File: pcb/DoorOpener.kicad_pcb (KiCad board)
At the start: 2 copper layers, 50.8 x 37.8 mm, 7 parts, among them SW1 POWER, SW2 Button, U2 ESP-01v090

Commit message: Prepare for milling the pcb
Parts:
- removed H2: MountingHole, MountingHole:MountingHole_3mm
- moved H1 14.6 mm to (76.0, 140.7)
- moved SW2 13.4 mm to (79.0, 125.6), turned to -90 degrees
- moved U2 8.07 mm to (84.1, 144.5)
- moved D1 7.12 mm to (85.0, 153.9)
- moved SW1 1.14 mm to (85.2, 124.6)
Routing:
- net Net-(SW2-Pad1): track 24.7 -> 16.0 mm
- net +3V3: track 31.5 -> 35.0 mm
- net Net-(D1-Pad4): track 16.5 -> 13.1 mm
- net Net-(BT1-Pad1): track 9.79 -> 8.40 mm
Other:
- board size 50.8 x 37.8 mm -> 48 x 37.7 mm
- board text added: "v0.1 - 17.11.2022"

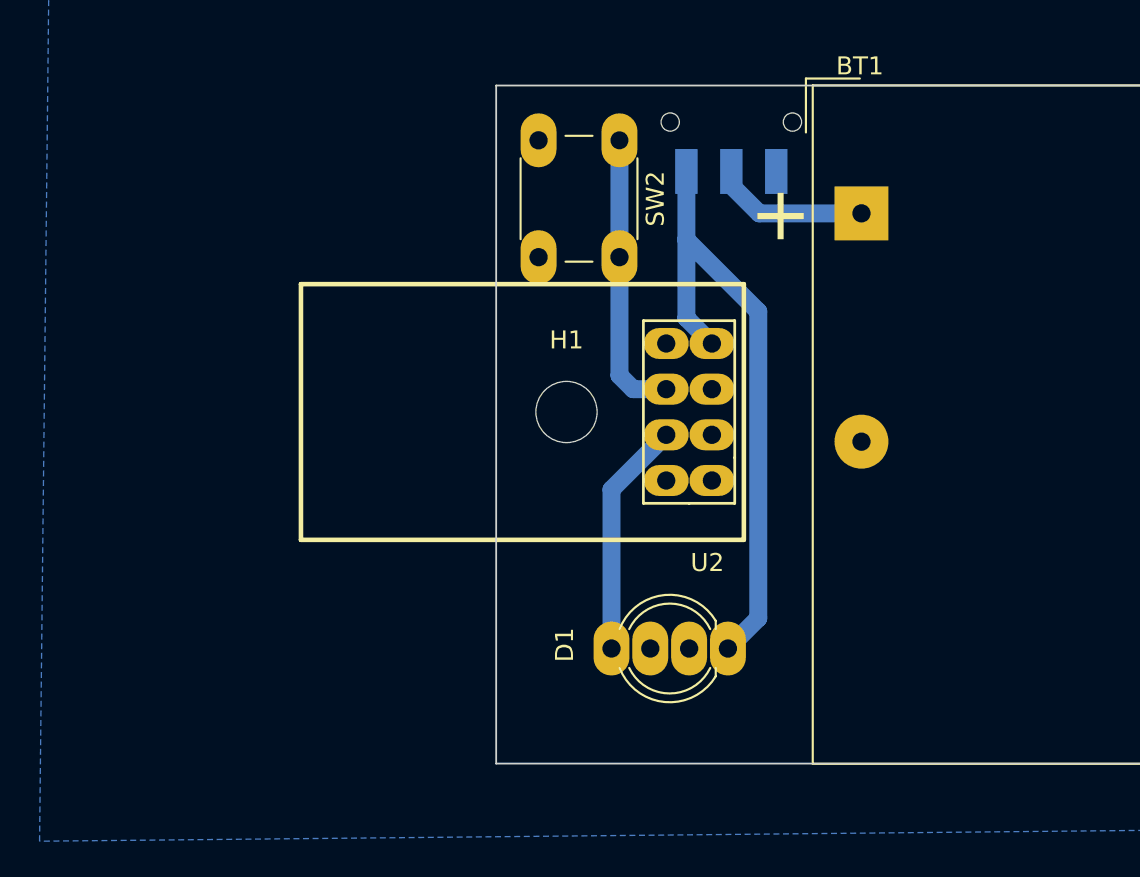
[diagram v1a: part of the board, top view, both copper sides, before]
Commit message: Add TX RX Connector
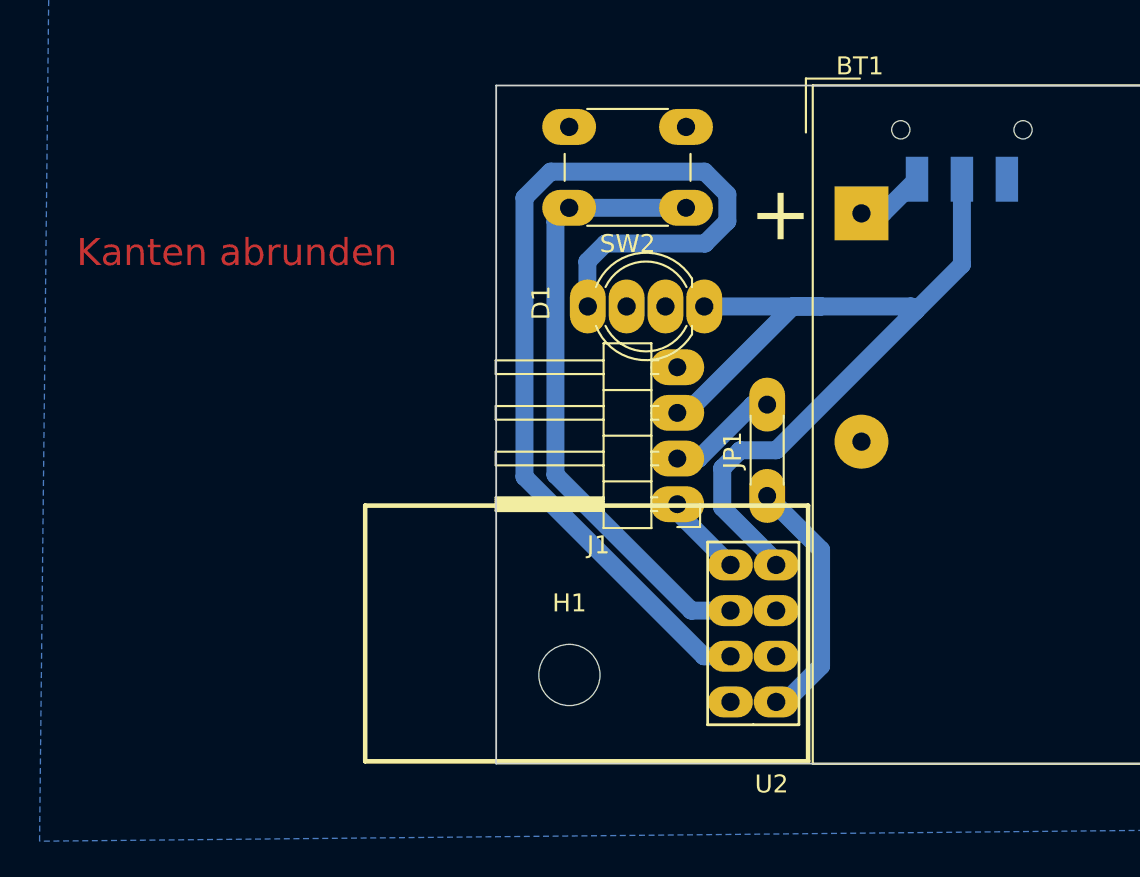
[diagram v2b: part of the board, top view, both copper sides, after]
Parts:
- added J1: Serial, Connector_PinHeader_2.54mm:PinHeader_1x04_P2.54mm_Horizontal, F.Cu at (82.2, 145.8)
- added JP1: Bridge, Resistor_THT:R_Axial_DIN0204_L3.6mm_D1.6mm_P5.08mm_Horizontal, F.Cu at (87.2, 145.4)
- moved D1 19.1 mm to (83.7, 134.8)
- moved H1 14.6 mm to (76.2, 155.3)
- moved SW1 12.8 mm to (98.0, 125.0)
- moved U2 12.8 mm to (87.7, 156.8)
- moved SW2 5.27 mm to (82.7, 129.4), turned to 180 degrees
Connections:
- SW1 pad 1: +3V3 -> Net-(BT1-Pad1)
- SW1 pad 2: Net-(BT1-Pad1) -> +3V3
- U2 pad 1: unconnected-(U2-Pad1) -> /TX
- U2 pad 8: unconnected-(U2-Pad8) -> /RX
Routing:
- net Net-(D1-Pad4): track 13.1 -> 55.7 mm
- net Net-(SW2-Pad1): track 16.0 -> 34.5 mm
- net +3V3: track 35.0 -> 51.7 mm
- net /TX: track 0.00 -> 14.0 mm
- net Net-(J1-Pad2): track 0.00 -> 6.13 mm
- net /RX: track 0.00 -> 4.61 mm
- net Net-(BT1-Pad1): track 8.40 -> 3.87 mm
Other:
- board text added: "Kanten abrunden"

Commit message: Version 0.2
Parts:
- removed H1: MountingHole, MountingHole:MountingHole_3mm
- moved SW1 1.86 mm to (96.2, 125.3)
- moved SW2 1.83 mm to (84.5, 129.4)
- moved JP1 1.46 mm to (88.4, 144.5)
- moved J1 1.02 mm to (81.8, 146.8)
- moved U2 0.89 mm to (87.7, 156.0)
- moved D1 0.25 mm to (83.8, 134.6)
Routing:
- net +3V3: track 51.7 -> 46.6 mm
- net Net-(D1-Pad4): track 55.7 -> 59.0 mm
- net Net-(J1-Pad2): track 6.13 -> 8.54 mm
- net Net-(BT1-Pad1): track 3.87 -> 2.09 mm
- net Net-(SW2-Pad1): track 34.5 -> 36.0 mm
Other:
- board size 48 x 37.7 mm -> 27.7 x 36.4 mm
- board text added: "v0.2 - 3.12.2022"
- board text removed: "Kanten abrunden"
- board text removed: "v0.1 - 17.11.2022"

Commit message: Minor adjustments
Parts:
- moved SW2 1.49 mm to (83.0, 129.4)
- moved J1 1.16 mm to (83.0, 146.8)
- moved U2 0.83 mm to (87.7, 156.8)
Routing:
- net Net-(D1-Pad4): track 59.0 -> 57.4 mm
- net Net-(SW2-Pad1): track 36.0 -> 34.7 mm
- net +3V3: track 46.6 -> 47.3 mm
- net /RX: track 4.86 -> 4.26 mm
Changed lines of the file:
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@@
   )
   (footprint "ESP8266:ESP-01" (layer "F.Cu")
-    (at 87.71 155.956 180)
+    (at 87.668318 156.782594 180)
     (descr "Module, ESP-8266, ESP-01, 8 pin")
     (tags "Module ESP-8266 ESP8266")
@@
   )
   (footprint "Button_Switch_THT:SW_PUSH_6mm_H4.3mm" (layer "F.Cu")
-    (at 84.53 129.357704 180)
+    (at 83.042691 129.357704 180)
     (descr "tactile push button, 6x6mm e.g. PHAP33xx series, height=4.3mm")
     (tags "tact sw push 6mm")
@@
   )
   (footprint "Connector_PinHeader_2.54mm:PinHeader_1x04_P2.54mm_Horizontal" (layer "F.Cu")
-    (at 81.845 146.802 180)
+    (at 83 146.802 180)
     (descr "Through hole angled pin header, 1x04, 2.54mm pitch, 6mm pin length, single row")
     (tags "Through hole angled pin header THT 1x04 2.54mm single row")
@@
     (effects (font (size 1.5 1.5) (thickness 0.25)))
   )
-  (segment (start 90.17 146.304) (end 88.392 144.526) (width 1) (layer "B.Cu") (net 3))
-  (segment (start 90.17 154.9732) (end 90.17 146.304) (width 1) (layer "B.Cu") (net 3))
-  (segment (start 87.71 155.956) (end 89.1872 155.956) (width 1) (layer "B.Cu") (net 3))
-  (segment (start 89.1872 155.956) (end 90.17 154.9732) (width 1) (layer "B.Cu") (net 3))
+  (segment (start 87.668318 156.782594) (end 89.145518 156.782594) (width 1) (layer "B.Cu") (net 3))
+  (segment (start 89.718318 156.209794) (end 89.718318 145.852318) (width 1) (layer "B.Cu") (net 3))
+  (segment (start 89.145518 156.782594) (end 89.718318 156.209794) (width 1) (layer "B.Cu") (net 3))
+  (segment (start 89.718318 145.852318) (end 88.392 144.526) (width 1) (layer "B.Cu") (net 3))
   (segment (start 92.456 129.3488) (end 93.71 128.0948) (width 1) (layer "B.Cu") (net 5))
   (segment (start 92.456 129.667) (end 92.456 129.3488) (width 1) (layer "B.Cu") (net 5))
+  (segment (start 86.38 138.847584) (end 86.38 134.62) (width 1) (layer "B.Cu") (net 7))
+  (segment (start 86.592 146.8316) (end 87.668318 147.907918) (width 1) (layer "B.Cu") (net 7))
   (segment (start 86.592 143.278) (end 88.124 141.746) (width 1) (layer "B.Cu") (net 7))
+  (segment (start 87.668318 147.907918) (end 87.668318 149.162594) (width 1) (layer "B.Cu") (net 7))
   (segment (start 86.592 146.8316) (end 86.592 143.278) (width 1) (layer "B.Cu") (net 7))
   (segment (start 88.124 141.746) (end 89.14 141.746) (width 1) (layer "B.Cu") (net 7))
-  (segment (start 87.71 148.336) (end 87.71 147.9496) (width 1) (layer "B.Cu") (net 7))
-  (segment (start 81.845 141.722) (end 82.350584 141.722) (width 1) (layer "B.Cu") (net 7))
+  (segment (start 83.82 134.62) (end 86.38 134.62) (width 1) (layer "B.Cu") (net 7))
   (segment (start 89.14 141.746) (end 96.21 134.676) (width 1) (layer "B.Cu") (net 7))
-  (segment (start 82.350584 141.722) (end 85.598 138.474584) (width 1) (layer "B.Cu") (net 7))
-  (segment (start 83.82 134.62) (end 96.154 134.62) (width 1) (layer "B.Cu") (net 7))
   (segment (start 96.21 134.676) (end 96.21 128.0948) (width 1) (layer "B.Cu") (net 7))
-  (segment (start 85.598 138.474584) (end 85.598 134.62) (width 1) (layer "B.Cu") (net 7))
-  (segment (start 87.71 147.9496) (end 86.592 146.8316) (width 1) (layer "B.Cu") (net 7))
+  (segment (start 83 141.722) (end 83.505584 141.722) (width 1) (layer "B.Cu") (net 7))
+  (segment (start 86.38 134.62) (end 96.154 134.62) (width 1) (layer "B.Cu") (net 7))
   (segment (start 96.154 134.62) (end 96.21 134.676) (width 1) (layer "B.Cu") (net 7))
+  (segment (start 83.505584 141.722) (end 86.38 138.847584) (width 1) (layer "B.Cu") (net 7))
+  (segment (start 74.168 128.524) (end 74.168 145.168) (width 1) (layer "B.Cu") (net 8))
+  (segment (start 78.138296 131.157704) (end 84.842296 131.157704) (width 1) (layer "B.Cu") (net 8))
+  (segment (start 74.168 145.168) (end 83.242594 154.242594) (width 1) (layer "B.Cu") (net 8))
   (segment (start 77.343 134.62) (end 77.343 131.953) (width 1) (layer "B.Cu") (net 8))
-  (segment (start 82.804 153.416) (end 85.17 153.416) (width 1) (layer "B.Cu") (net 8))
-  (segment (start 74.168 144.78) (end 82.804 153.416) (width 1) (layer "B.Cu") (net 8))
-  (segment (start 74.168 128.524) (end 74.168 144.78) (width 1) (layer "B.Cu") (net 8))
-  (segment (start 77.978 131.318) (end 85.852 131.318) (width 1) (layer "B.Cu") (net 8))
-  (segment (start 77.343 131.953) (end 77.978 131.318) (width 1) (layer "B.Cu") (net 8))
-  (segment (start 86.868 128.65012) (end 85.72588 127.508) (width 1) (layer "B.Cu") (net 8))
-  (segment (start 86.868 130.302) (end 86.868 128.65012) (width 1) (layer "B.Cu") (net 8))
-  (segment (start 85.72588 127.508) (end 75.184 127.508) (width 1) (layer "B.Cu") (net 8))
-  (segment (start 85.852 131.318) (end 86.868 130.302) (width 1) (layer "B.Cu") (net 8))
+  (segment (start 77.343 131.953) (end 78.138296 131.157704) (width 1) (layer "B.Cu") (net 8))
   (segment (start 75.184 127.508) (end 74.168 128.524) (width 1) (layer "B.Cu") (net 8))
-  (segment (start 85.17 148.336) (end 83.379 148.336) (width 1) (layer "B.Cu") (net 9))
-  (segment (start 83.379 148.336) (end 81.845 146.802) (width 1) (layer "B.Cu") (net 9))
-  (segment (start 81.845 146.802) (end 82.7472 146.802) (width 1) (layer "B.Cu") (net 9))
-  (segment (start 78.03 129.357704) (end 76.196116 129.357704) (width 1) (layer "B.Cu") (net 10))
-  (segment (start 75.467501 144.241729) (end 82.101772 150.876) (width 1) (layer "B.Cu") (net 10))
-  (segment (start 76.196116 129.357704) (end 75.467501 130.086319) (width 1) (layer "B.Cu") (net 10))
-  (segment (start 78.03 129.357704) (end 84.53 129.357704) (width 1) (layer "B.Cu") (net 10))
-  (segment (start 82.101772 150.876) (end 85.17 150.876) (width 1) (layer "B.Cu") (net 10))
-  (segment (start 75.467501 130.086319) (end 75.467501 144.241729) (width 1) (layer "B.Cu") (net 10))
+  (segment (start 83.242594 154.242594) (end 85.128318 154.242594) (width 1) (layer "B.Cu") (net 8))
+  (segment (start 84.842296 131.157704) (end 86 130) (width 1) (layer "B.Cu") (net 8))
+  (segment (start 86 129) (end 84.508 127.508) (width 1) (layer "B.Cu") (net 8))
+  (segment (start 86 130) (end 86 129) (width 1) (layer "B.Cu") (net 8))
+  (segment (start 84.508 127.508) (end 75.184 127.508) (width 1) (layer "B.Cu") (net 8))
+  (segment (start 81.845 146.802) (end 82.767724 146.802) (width 1) (layer "B.Cu") (net 9))
+  (segment (start 82.767724 146.802) (end 85.128318 149.162594) (width 1) (layer "B.Cu") (net 9))
+  (segment (start 75.467501 130.432894) (end 75.467501 144.467501) (width 1) (layer "B.Cu") (net 10))
+  (segment (start 76.542691 129.357704) (end 75.467501 130.432894) (width 1) (layer "B.Cu") (net 10))
+  (segment (start 76.542691 129.357704) (end 83.042691 129.357704) (width 1) (layer "B.Cu") (net 10))
+  (segment (start 75.467501 144.467501) (end 82.702594 151.702594) (width 1) (layer "B.Cu") (net 10))
+  (segment (start 82.702594 151.702594) (end 85.128318 151.702594) (width 1) (layer "B.Cu") (net 10))
   (segment (start 83.576 144.262) (end 88.392 139.446) (width 1) (layer "B.Cu") (net 11))
   (segment (start 81.845 144.262) (end 83.576 144.262) (width 1) (layer "B.Cu") (net 11))
